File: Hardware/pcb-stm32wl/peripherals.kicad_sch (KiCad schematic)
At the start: 50 parts, among them J10 Qwiic, J8 DEBUG, J9 UART/I2C, Q2 PMST4401,115, SW1 USR_BTN, SW2 RESET, U10 SHTC3, U11 ATECC608B-TNGLORAU, U8 MX25R1635, U9 LIS2DH12

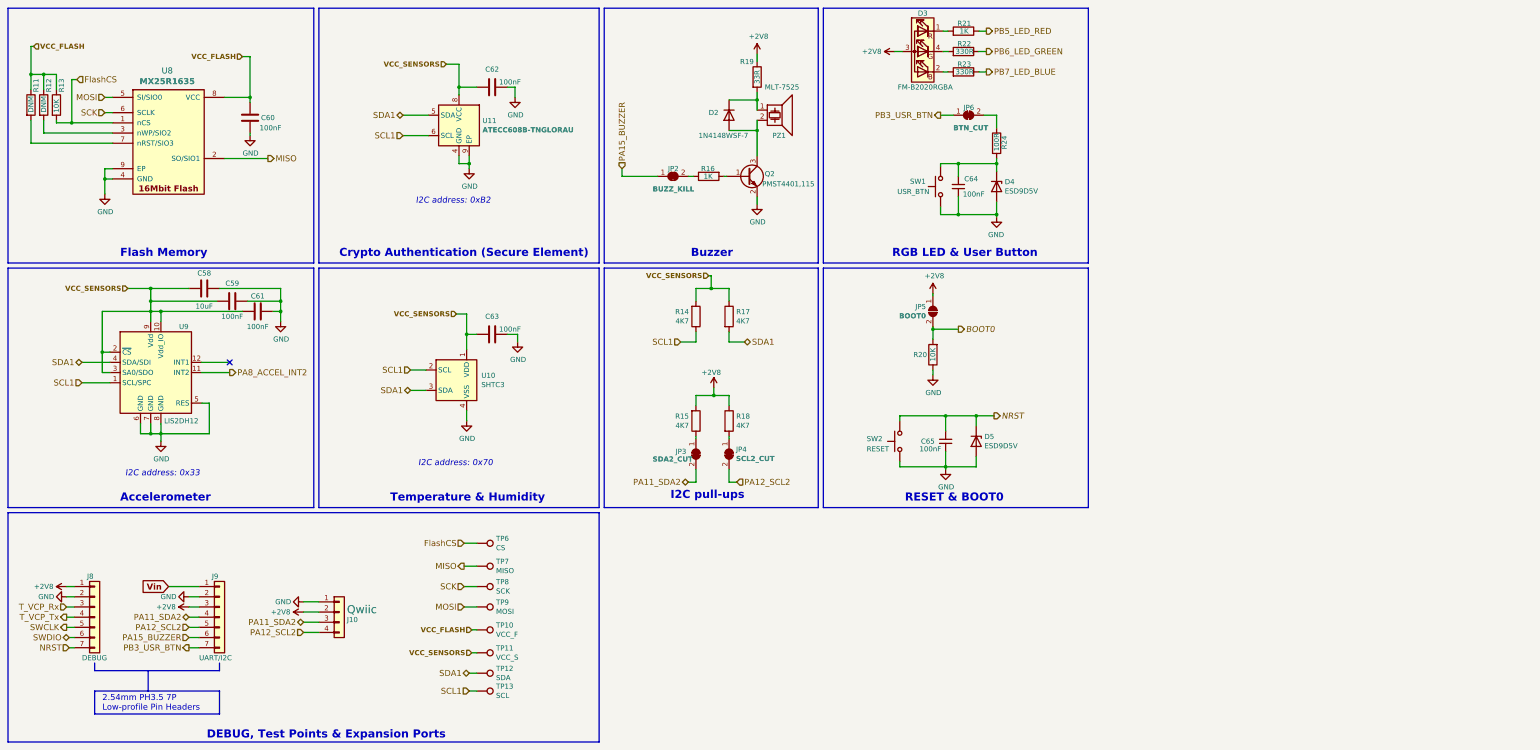
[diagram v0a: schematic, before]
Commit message: updated strain gauge connections and created todo tasks
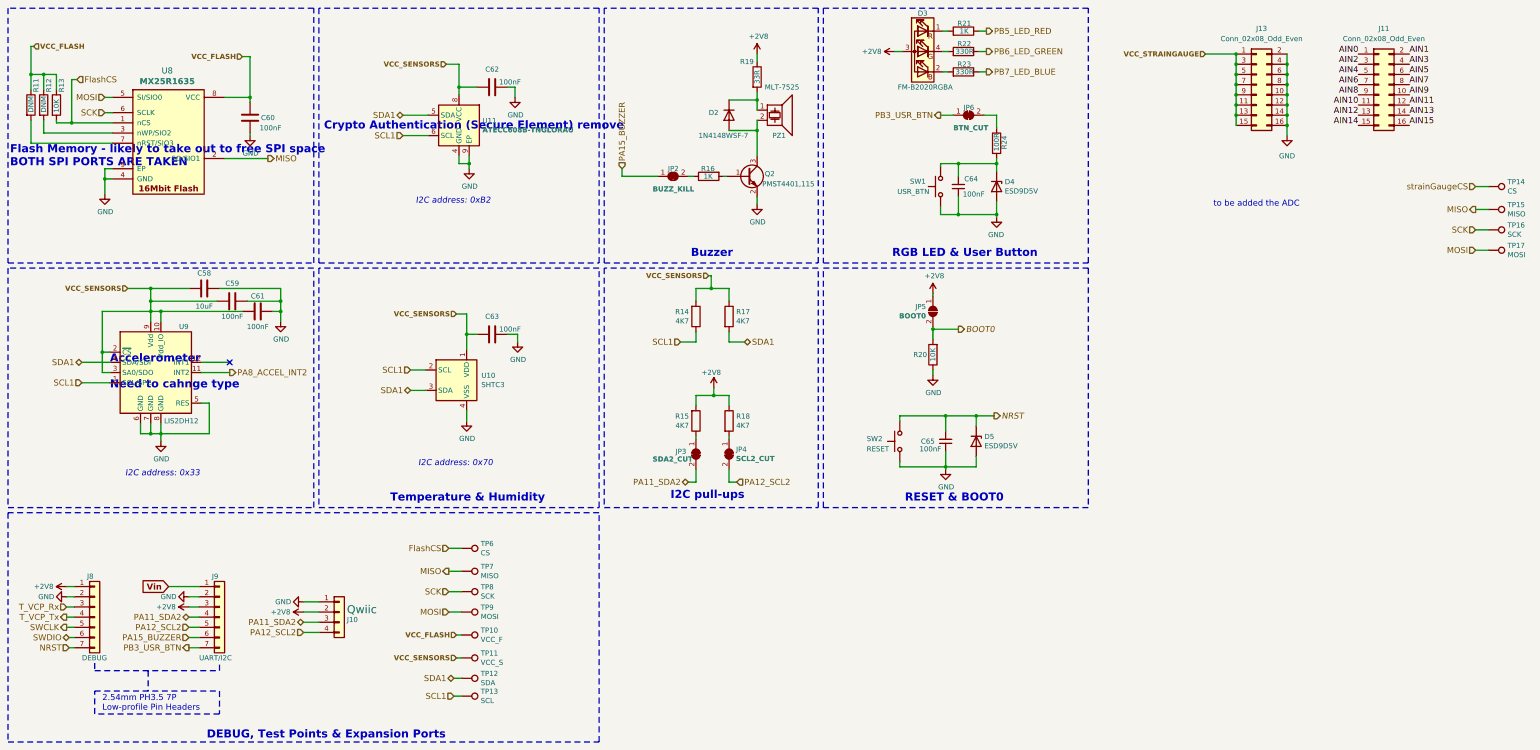
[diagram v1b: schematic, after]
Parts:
- added J11, J13: Conn_02x08_Odd_Even, symbol Connector_Generic:Conn_02x08_Odd_Even
- added TP14: CS, TestPoint:TestPoint_Pad_D1.5mm, symbol Connector:TestPoint
- added TP15: MISO, TestPoint:TestPoint_Pad_D1.5mm, symbol Connector:TestPoint
- added TP16: SCK, TestPoint:TestPoint_Pad_D1.5mm, symbol Connector:TestPoint
- added TP17: MOSI, TestPoint:TestPoint_Pad_D1.5mm, symbol Connector:TestPoint
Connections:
- net GND: now also J13.10 (Pin_10), J13.12 (Pin_12), J13.14 (Pin_14), J13.16 (Pin_16), J13.2 (Pin_2), J13.4 (Pin_4), J13.6 (Pin_6), J13.8 (Pin_8)
- net MISO: now also TP15.1
- net MOSI: now also TP17.1
- net SCK: now also TP16.1
- new net AIN0: J11.1 (Pin_1)
- new net AIN1: J11.2 (Pin_2)
- new net AIN10: J11.11 (Pin_11)
- new net AIN11: J11.12 (Pin_12)
- new net AIN12: J11.13 (Pin_13)
- new net AIN13: J11.14 (Pin_14)
- new net AIN14: J11.15 (Pin_15)
- new net AIN15: J11.16 (Pin_16)
- new net AIN2: J11.3 (Pin_3)
- new net AIN3: J11.4 (Pin_4)
- new net AIN4: J11.5 (Pin_5)
- new net AIN5: J11.6 (Pin_6)
- new net AIN6: J11.7 (Pin_7)
- new net AIN7: J11.8 (Pin_8)
- new net AIN8: J11.9 (Pin_9)
- new net AIN9: J11.10 (Pin_10)
- new net VCC_STRAINGAUGE: J13.1 (Pin_1), J13.11 (Pin_11), J13.13 (Pin_13), J13.15 (Pin_15), J13.3 (Pin_3), J13.5 (Pin_5), J13.7 (Pin_7), J13.9 (Pin_9)
- new net strainGaugeCS: TP14.1
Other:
- note added: "Accelerometer Need to cahnge type"
- note added: "Crypto Authentication (Secure Element) remove"
- note added: "Flash Memory - likely to take out to free SPI space BOTH SPI PORTS ARE TAKEN"
- note added: "to be added the ADC"
- note removed: "Accelerometer"
- note removed: "Crypto Authentication (Secure Element)"
- note removed: "Flash Memory"
- company: The Things Industries -> BCIT BAJA
- moved on the sheet: TP10, TP11, TP12, TP13, TP6, TP7, TP8, TP9
